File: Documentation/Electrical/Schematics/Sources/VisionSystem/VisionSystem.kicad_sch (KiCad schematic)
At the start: 11 parts

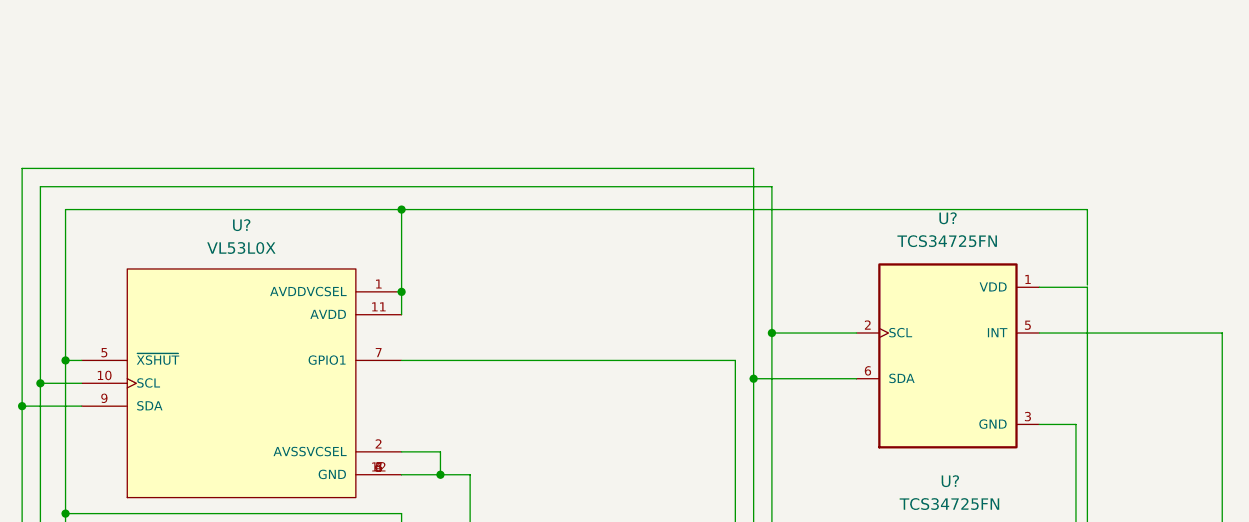
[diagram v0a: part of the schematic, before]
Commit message: more specific and added Pull up resistor
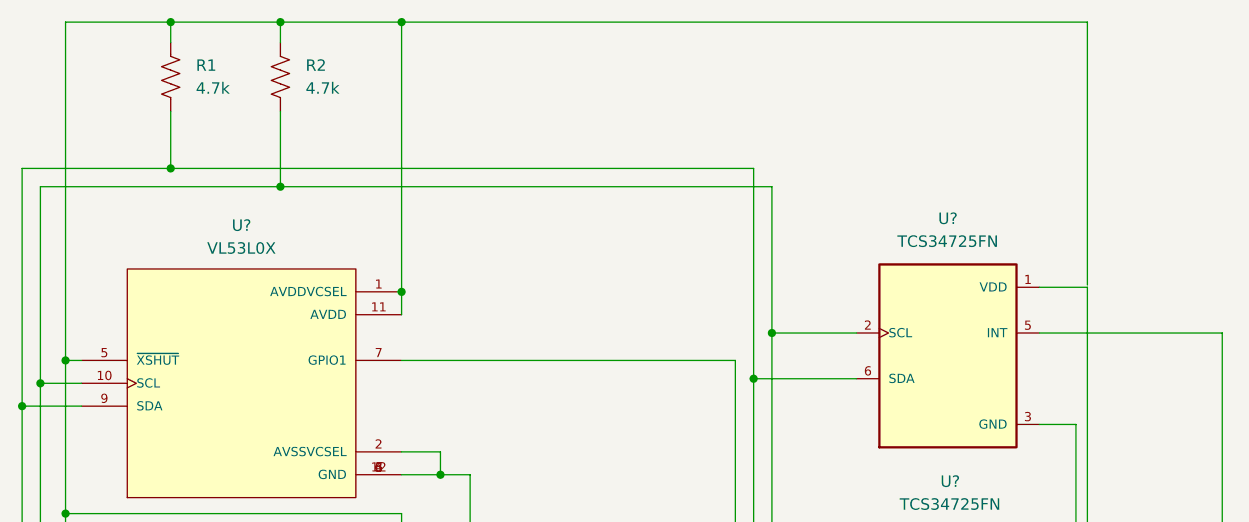
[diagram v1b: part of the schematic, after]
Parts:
- added R1, R2: 4.7k, symbol Device:R_US
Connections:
- net at U?.1 (AVDDVCSEL), U?.1 (AVDDVCSEL), U?.1 (AVDDVCSEL)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: now also R1.1, R2.1
- net at J?.I2C_2_SCL, U?.10 (SCL), U?.10 (SCL)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: now also R2.2
- net at J?.I2C_2_SDA, U?.6 (SDA), U?.6 (SDA)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: now also R1.2
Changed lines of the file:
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@@
   (junction (at 169.926 161.036) (diameter 0) (color 0 0 0 0)
   )
+  (junction (at 144.272 61.976) (diameter 0) (color 0 0 0 0)
+  )
   (junction (at 173.736 320.294) (diameter 0) (color 0 0 0 0)
   )
+  (junction (at 144.272 78.232) (diameter 0) (color 0 0 0 0)
+  )
   (junction (at 129.794 102.108) (diameter 0) (color 0 0 0 0)
   )
+  (junction (at 156.464 80.264) (diameter 0) (color 0 0 0 0)
+  )
   (junction (at 127.762 279.4) (diameter 0) (color 0 0 0 0)
   )
@@
   (junction (at 244.856 135.89) (diameter 0) (color 0 0 0 0)
   )
-  (junction (at 169.926 82.804) (diameter 0) (color 0 0 0 0)
-  )
   (junction (at 169.926 125.73) (diameter 0) (color 0 0 0 0)
   )
   (junction (at 173.736 355.092) (diameter 0) (color 0 0 0 0)
   )
+  (junction (at 156.464 61.976) (diameter 0) (color 0 0 0 0)
+  )
   (junction (at 211.074 96.52) (diameter 0) (color 0 0 0 0)
   )
@@
   (junction (at 127.762 244.094) (diameter 0) (color 0 0 0 0)
   )
+  (junction (at 169.926 61.976) (diameter 0) (color 0 0 0 0)
+  )
   (junction (at 132.588 168.656) (diameter 0) (color 0 0 0 0)
   )
@@
     (stroke (width 0) (type default) (color 0 0 0 0))
   )
+  (wire (pts (xy 144.272 78.232) (xy 209.042 78.232))
+    (stroke (width 0) (type default) (color 0 0 0 0))
+  )
   (wire (pts (xy 127.762 244.094) (xy 127.762 279.4))
     (stroke (width 0) (type default) (color 0 0 0 0))
@@
     (stroke (width 0) (type default) (color 0 0 0 0))
   )
+  (wire (pts (xy 156.464 61.976) (xy 169.926 61.976))
+    (stroke (width 0) (type default) (color 0 0 0 0))
+  )
+  (wire (pts (xy 156.464 80.264) (xy 211.074 80.264))
+    (stroke (width 0) (type default) (color 0 0 0 0))
+  )
   (wire (pts (xy 127.762 78.232) (xy 127.762 104.648))
     (stroke (width 0) (type default) (color 0 0 0 0))
@@
     (stroke (width 0) (type default) (color 0 0 0 0))
   )
-  (wire (pts (xy 132.588 82.804) (xy 132.588 99.568))
+  (wire (pts (xy 132.588 61.976) (xy 132.588 99.568))
     (stroke (width 0) (type default) (color 0 0 0 0))
   )
@@
     (stroke (width 0) (type default) (color 0 0 0 0))
   )
-  (wire (pts (xy 169.926 82.804) (xy 169.926 91.948))
-    (stroke (width 0) (type default) (color 0 0 0 0))
-  )
   (wire (pts (xy 177.546 320.294) (xy 177.546 355.092))
     (stroke (width 0) (type default) (color 0 0 0 0))
@@
     (stroke (width 0) (type default) (color 0 0 0 0))
   )
+  (wire (pts (xy 144.272 61.976) (xy 156.464 61.976))
+    (stroke (width 0) (type default) (color 0 0 0 0))
+  )
   (wire (pts (xy 301.752 171.704) (xy 312.674 171.704))
     (stroke (width 0) (type default) (color 0 0 0 0))
   )
-  (wire (pts (xy 246.126 91.186) (xy 246.126 82.804))
+  (wire (pts (xy 246.126 91.186) (xy 246.126 61.976))
+    (stroke (width 0) (type default) (color 0 0 0 0))
+  )
+  (wire (pts (xy 144.272 61.976) (xy 144.272 64.262))
     (stroke (width 0) (type default) (color 0 0 0 0))
   )
@@
     (stroke (width 0) (type default) (color 0 0 0 0))
   )
-  (wire (pts (xy 132.588 82.804) (xy 169.926 82.804))
+  (wire (pts (xy 144.272 71.882) (xy 144.272 78.232))
+    (stroke (width 0) (type default) (color 0 0 0 0))
+  )
+  (wire (pts (xy 132.588 61.976) (xy 144.272 61.976))
     (stroke (width 0) (type default) (color 0 0 0 0))
   )
@@
     (stroke (width 0) (type default) (color 0 0 0 0))
   )
-  (wire (pts (xy 246.126 82.804) (xy 169.926 82.804))
+  (wire (pts (xy 246.126 61.976) (xy 169.926 61.976))
     (stroke (width 0) (type default) (color 0 0 0 0))
   )
@@
     (stroke (width 0) (type default) (color 0 0 0 0))
   )
+  (wire (pts (xy 156.464 64.262) (xy 156.464 61.976))
+    (stroke (width 0) (type default) (color 0 0 0 0))
+  )
   (wire (pts (xy 174.244 112.268) (xy 177.546 112.268))
     (stroke (width 0) (type default) (color 0 0 0 0))
@@
     (stroke (width 0) (type default) (color 0 0 0 0))
   )
+  (wire (pts (xy 169.926 61.976) (xy 169.926 91.948))
+    (stroke (width 0) (type default) (color 0 0 0 0))
+  )
   (wire (pts (xy 261.112 96.52) (xy 261.112 204.724))
     (stroke (width 0) (type default) (color 0 0 0 0))
@@
     (stroke (width 0) (type default) (color 0 0 0 0))
   )
-  (wire (pts (xy 209.042 78.232) (xy 127.762 78.232))
-    (stroke (width 0) (type default) (color 0 0 0 0))
-  )
-  (wire (pts (xy 129.794 80.264) (xy 211.074 80.264))
+  (wire (pts (xy 127.762 78.232) (xy 144.272 78.232))
+    (stroke (width 0) (type default) (color 0 0 0 0))
+  )
+  (wire (pts (xy 129.794 80.264) (xy 156.464 80.264))
     (stroke (width 0) (type default) (color 0 0 0 0))
   )
@@
   )
   (wire (pts (xy 240.792 96.52) (xy 261.112 96.52))
+    (stroke (width 0) (type default) (color 0 0 0 0))
+  )
+  (wire (pts (xy 156.464 71.882) (xy 156.464 80.264))
     (stroke (width 0) (type default) (color 0 0 0 0))
   )
@@
     (pin "5")
     (pin "6")
+  )
+  (symbol (lib_id "Device:R_US") (at 144.272 68.072 0) (unit 1)
+    (in_bom yes) (on_board yes) (fields_autoplaced)
+    (property "Reference" "R1" (id 0) (at 147.066 66.8019 0)
+      (effects (font (size 1.27 1.27)) (justify left))
+    )
+    (property "Value" "4.7k" (id 1) (at 147.066 69.3419 0)
+      (effects (font (size 1.27 1.27)) (justify left))
+    )
+    (property "Footprint" "" (id 2) (at 145.288 68.326 90)
+      (effects (font (size 1.27 1.27)) hide)
+    )
+    (property "Datasheet" "~" (id 3) (at 144.272 68.072 0)
+      (effects (font (size 1.27 1.27)) hide)
+    )
+    (pin "1")
+    (pin "2")
   )
   (symbol (lib_id "VL53L0X:VL53L0X") (at 152.146 102.108 0) (unit 1)
@@
     (pin "9")
   )
+  (symbol (lib_id "Device:R_US") (at 156.464 68.072 0) (unit 1)
+    (in_bom yes) (on_board yes) (fields_autoplaced)
+    (property "Reference" "R2" (id 0) (at 159.258 66.8019 0)
+      (effects (font (size 1.27 1.27)) (justify left))
+    )
+    (property "Value" "4.7k" (id 1) (at 159.258 69.3419 0)
+      (effects (font (size 1.27 1.27)) (justify left))
+    )
+    (property "Footprint" "" (id 2) (at 157.48 68.326 90)
+      (effects (font (size 1.27 1.27)) hide)
+    )
+    (property "Datasheet" "~" (id 3) (at 156.464 68.072 0)
+      (effects (font (size 1.27 1.27)) hide)
+    )
+    (pin "1")
+    (pin "2")
+  )
   (symbol (lib_id "TCS34725FN:TCS34725FN") (at 230.886 128.27 0) (unit 1)
     (in_bom yes) (on_board yes) (fields_autoplaced)
@@
       (reference "J?") (unit 1) (value "Jetson Nano 40 pin Header") (footprint "")
     )
+    (path "/5302f359-78ac-4ee8-97b6-ae3b7e9235ea"
+      (reference "R1") (unit 1) (value "4.7k") (footprint "")
+    )
+    (path "/df96cf9b-8aa7-4c73-99e0-a07b94490858"
+      (reference "R2") (unit 1) (value "4.7k") (footprint "")
+    )
     (path "/12c943ec-a0d1-4282-a073-8e9c93908e26"

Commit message: fixed schematic
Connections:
- net at R1.1, R2.1, U?.1 (AVDDVCSEL)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: now also U?.1 (AVDDVCSEL), U?.1 (AVDDVCSEL), U?.1 (AVDDVCSEL), U?.11 (AVDD), U?.11 (AVDD), U?.11 (AVDD), U?.5 (~{XSHUT}), U?.5 (~{XSHUT}), U?.5 (~{XSHUT})
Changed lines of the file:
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@@
   (junction (at 177.546 355.092) (diameter 0) (color 0 0 0 0)
   )
+  (junction (at 132.588 257.556) (diameter 0) (color 0 0 0 0)
+  )
   (junction (at 127.762 173.736) (diameter 0) (color 0 0 0 0)
   )
@@
   (junction (at 127.762 209.042) (diameter 0) (color 0 0 0 0)
   )
+  (junction (at 132.588 239.014) (diameter 0) (color 0 0 0 0)
+  )
   (junction (at 177.546 216.662) (diameter 0) (color 0 0 0 0)
   )
@@
     (stroke (width 0) (type default) (color 0 0 0 0))
   )
-  (wire (pts (xy 132.588 274.32) (xy 132.588 257.556))
+  (wire (pts (xy 132.588 239.014) (xy 132.588 257.556))
     (stroke (width 0) (type default) (color 0 0 0 0))
   )
@@
     (stroke (width 0) (type default) (color 0 0 0 0))
   )
+  (wire (pts (xy 132.588 257.556) (xy 132.588 274.32))
+    (stroke (width 0) (type default) (color 0 0 0 0))
+  )
